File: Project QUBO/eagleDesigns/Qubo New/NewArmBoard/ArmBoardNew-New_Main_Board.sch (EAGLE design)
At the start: 13 parts, among them U1 BME280

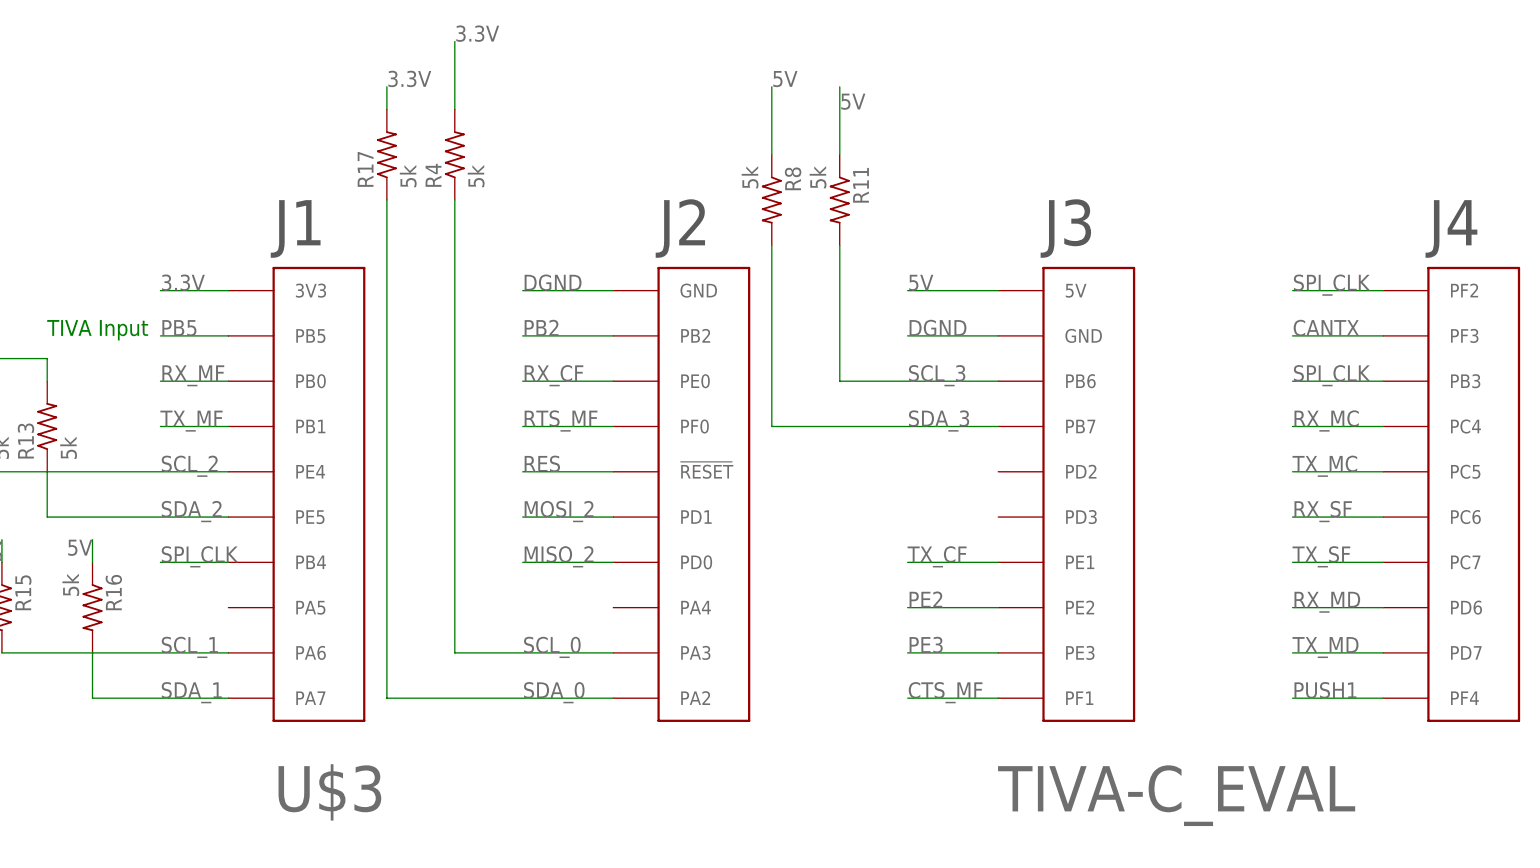
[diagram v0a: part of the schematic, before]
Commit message: Fixes to TIVA board
Some of the pins were named wrong so I fixed them
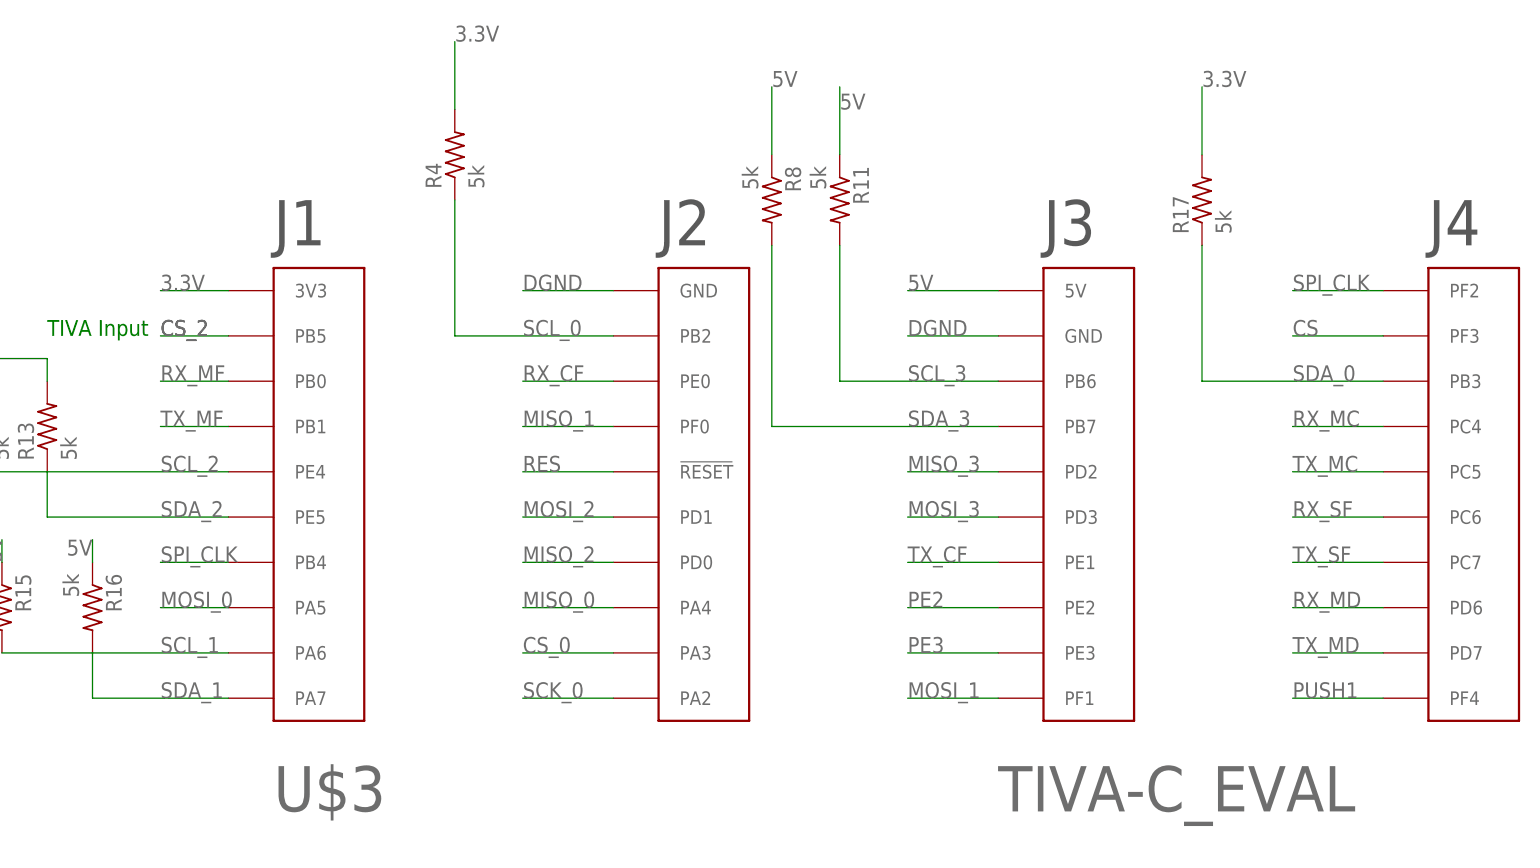
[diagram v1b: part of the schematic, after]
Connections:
- net CANTX renamed CS
- net CTS_MF renamed MOSI_1
- net PB5 renamed CS_2
- net RTS_MF renamed MISO_1
- removed net PB2: U$3.PB2
- new net CS_0: U$3.PA3
- new net MISO_0: U$3.PA4
- new net MISO_3: U$3.PD2
- new net MOSI_0: U$3.PA5
- new net MOSI_3: U$3.PD3
- new net SCK_0: U$3.PA2
- net SCL_0: now also U$3.PB2; no longer U$3.PA3
- net SDA_0: now also U$3.PB3; no longer U$3.PA2
- net SPI_CLK: no longer U$3.PB3
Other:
- moved on the sheet: R17
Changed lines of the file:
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@@
 <instance part="R8" gate="G$1" x="223.52" y="190.5" rot="R270"/>
 <instance part="R11" gate="G$1" x="231.14" y="190.5" rot="R270"/>
-<instance part="R17" gate="G$1" x="180.34" y="195.58" rot="R90"/>
+<instance part="R17" gate="G$1" x="271.78" y="190.5" rot="R90"/>
 <instance part="JP1" gate="G$1" x="101.6" y="144.78"/>
 </instances>
@@
 </busses>
 <nets>
-<net name="PB5" class="0">
+<net name="CS_2" class="0">
 <segment>
 <pinref part="U$3" gate="G$1" pin="PB5"/>
 <wire x1="162.56" y1="175.26" x2="154.94" y2="175.26" width="0.1524" layer="91"/>
+<label x="154.94" y="175.26" size="1.778" layer="95"/>
 <label x="154.94" y="175.26" size="1.778" layer="95"/>
 </segment>
@@
 <label x="281.94" y="180.34" size="1.778" layer="95"/>
 </segment>
-<segment>
-<pinref part="U$3" gate="G$1" pin="PB3"/>
-<wire x1="292.1" y1="170.18" x2="281.94" y2="170.18" width="0.1524" layer="91"/>
-<label x="281.94" y="170.18" size="1.778" layer="95"/>
-</segment>
 </net>
 <net name="RX_MF" class="0">
@@
 <segment>
 <pinref part="R17" gate="G$1" pin="2"/>
-<wire x1="180.34" y1="200.66" x2="180.34" y2="203.2" width="0.1524" layer="91"/>
-<label x="180.34" y="203.2" size="1.778" layer="95"/>
+<wire x1="271.78" y1="195.58" x2="271.78" y2="203.2" width="0.1524" layer="91"/>
+<label x="271.78" y="203.2" size="1.778" layer="95"/>
 </segment>
 <segment>
@@
 </segment>
 </net>
-<net name="CTS_MF" class="0">
+<net name="MOSI_1" class="0">
 <segment>
 <pinref part="U$3" gate="G$1" pin="PF1"/>
@@
 </segment>
 </net>
-<net name="RTS_MF" class="0">
+<net name="MISO_1" class="0">
 <segment>
 <pinref part="U$3" gate="G$1" pin="PF0"/>
@@
 </segment>
 </net>
-<net name="CANTX" class="0">
+<net name="CS" class="0">
 <segment>
 <pinref part="U$3" gate="G$1" pin="PF3"/>
@@
 </segment>
 <segment>
-<pinref part="U$3" gate="G$1" pin="PA3"/>
-<wire x1="205.74" y1="139.7" x2="187.96" y2="139.7" width="0.1524" layer="91"/>
-<label x="195.58" y="139.7" size="1.778" layer="95"/>
+<pinref part="U$3" gate="G$1" pin="PB2"/>
+<wire x1="205.74" y1="175.26" x2="187.96" y2="175.26" width="0.1524" layer="91"/>
+<label x="195.58" y="175.26" size="1.778" layer="95"/>
 <pinref part="R4" gate="G$1" pin="1"/>
-<wire x1="187.96" y1="190.5" x2="187.96" y2="139.7" width="0.1524" layer="91"/>
+<wire x1="187.96" y1="190.5" x2="187.96" y2="175.26" width="0.1524" layer="91"/>
 </segment>
 </net>
@@
 </segment>
 <segment>
-<pinref part="U$3" gate="G$1" pin="PA2"/>
-<label x="195.58" y="134.62" size="1.778" layer="95"/>
-<wire x1="205.74" y1="134.62" x2="180.34" y2="134.62" width="0.1524" layer="91"/>
+<pinref part="U$3" gate="G$1" pin="PB3"/>
+<label x="281.94" y="170.18" size="1.778" layer="95"/>
 <pinref part="R17" gate="G$1" pin="1"/>
-<wire x1="180.34" y1="134.62" x2="180.34" y2="190.5" width="0.1524" layer="91"/>
+<wire x1="271.78" y1="185.42" x2="271.78" y2="170.18" width="0.1524" layer="91"/>
+<wire x1="271.78" y1="170.18" x2="292.1" y2="170.18" width="0.1524" layer="91"/>
 </segment>
 </net>
@@
 </segment>
 </net>
-<net name="PB2" class="0">
-<segment>
-<pinref part="U$3" gate="G$1" pin="PB2"/>
-<wire x1="205.74" y1="175.26" x2="195.58" y2="175.26" width="0.1524" layer="91"/>
-<label x="195.58" y="175.26" size="1.778" layer="95"/>
-</segment>
-</net>
+<net name="MISO_3" class="0">
+<segment>
+<pinref part="U$3" gate="G$1" pin="PD2"/>
+<wire x1="248.92" y1="160.02" x2="238.76" y2="160.02" width="0.1524" layer="91"/>
+<label x="238.76" y="160.02" size="1.778" layer="95"/>
+</segment>
+</net>
+<net name="MOSI_3" class="0">
+<segment>
+<pinref part="U$3" gate="G$1" pin="PD3"/>
+<wire x1="248.92" y1="154.94" x2="238.76" y2="154.94" width="0.1524" layer="91"/>
+<label x="238.76" y="154.94" size="1.778" layer="95"/>
+</segment>
+</net>
+<net name="MISO_0" class="0">
+<segment>
+<pinref part="U$3" gate="G$1" pin="PA4"/>
+<wire x1="205.74" y1="144.78" x2="195.58" y2="144.78" width="0.1524" layer="91"/>
+<label x="195.58" y="144.78" size="1.778" layer="95"/>
+</segment>
+</net>
+<net name="CS_0" class="0">
+<segment>
+<pinref part="U$3" gate="G$1" pin="PA3"/>
+<wire x1="205.74" y1="139.7" x2="195.58" y2="139.7" width="0.1524" layer="91"/>
+<label x="195.58" y="139.7" size="1.778" layer="95"/>
+</segment>
+</net>
+<net name="SCK_0" class="0">
+<segment>
+<pinref part="U$3" gate="G$1" pin="PA2"/>
+<wire x1="205.74" y1="134.62" x2="195.58" y2="134.62" width="0.1524" layer="91"/>
+<label x="195.58" y="134.62" size="1.778" layer="95"/>
+</segment>
+</net>
+<net name="MOSI_0" class="0">
+<segment>
+<pinref part="U$3" gate="G$1" pin="PA5"/>
+<wire x1="162.56" y1="144.78" x2="154.94" y2="144.78" width="0.1524" layer="91"/>
+<label x="154.94" y="144.78" size="1.778" layer="95"/>
+</segment>
+</net>

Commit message: Changes to Tiva board
I had to rewire some things
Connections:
- new net SPI_CLK_2: U$3.PB4
- net 3.3V: now also R15.1, R16.1, U$1.9; no longer R17.2, R4.2
- net 5V: now also R17.2, R4.2; no longer R15.1, R16.1
- net N$9: no longer U$1.9
- net SCL_0: no longer U1.SCK/SCL
- net SCL_1: now also U1.SCK/SCL
- net SDA_0: no longer U1.SDI/SDA
- net SDA_1: now also U1.SDI/SDA
- net SPI_CLK: no longer U$3.PB4
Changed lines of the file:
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@@
 <net name="SPI_CLK" class="0">
-<segment>
-<pinref part="U$3" gate="G$1" pin="PB4"/>
-<wire x1="162.56" y1="149.86" x2="154.94" y2="149.86" width="0.1524" layer="91"/>
-<label x="154.94" y="149.86" size="1.778" layer="95"/>
-</segment>
 <segment>
 <pinref part="U$3" gate="G$1" pin="PF2"/>
@@
 </segment>
 <segment>
-<pinref part="R17" gate="G$1" pin="2"/>
-<wire x1="271.78" y1="195.58" x2="271.78" y2="203.2" width="0.1524" layer="91"/>
-<label x="271.78" y="203.2" size="1.778" layer="95"/>
-</segment>
-<segment>
-<pinref part="R4" gate="G$1" pin="2"/>
-<wire x1="187.96" y1="200.66" x2="187.96" y2="208.28" width="0.1524" layer="91"/>
-<label x="187.96" y="208.28" size="1.778" layer="95"/>
+<wire x1="147.32" y1="149.86" x2="147.32" y2="152.4" width="0.1524" layer="91"/>
+<label x="147.32" y="152.4" size="1.778" layer="95" rot="R180"/>
+<pinref part="R16" gate="G$1" pin="1"/>
+</segment>
+<segment>
+<wire x1="137.16" y1="149.86" x2="137.16" y2="152.4" width="0.1524" layer="91"/>
+<label x="137.16" y="149.86" size="1.778" layer="95" rot="R90"/>
+<pinref part="R15" gate="G$1" pin="1"/>
+</segment>
+<segment>
+<pinref part="U$1" gate="G$1" pin="9"/>
+<wire x1="177.8" y1="48.26" x2="170.18" y2="48.26" width="0.1524" layer="91"/>
+<label x="170.18" y="48.26" size="1.778" layer="95"/>
 </segment>
 </net>
@@
 </segment>
 <segment>
-<wire x1="137.16" y1="149.86" x2="137.16" y2="152.4" width="0.1524" layer="91"/>
-<label x="137.16" y="149.86" size="1.778" layer="95" rot="R90"/>
-<pinref part="R15" gate="G$1" pin="1"/>
-</segment>
-<segment>
-<wire x1="147.32" y1="149.86" x2="147.32" y2="152.4" width="0.1524" layer="91"/>
-<label x="147.32" y="152.4" size="1.778" layer="95" rot="R180"/>
-<pinref part="R16" gate="G$1" pin="1"/>
-</segment>
-<segment>
 <pinref part="U$3" gate="G$1" pin="5V"/>
 <wire x1="248.92" y1="180.34" x2="238.76" y2="180.34" width="0.1524" layer="91"/>
@@
 <label x="88.9" y="147.32" size="1.778" layer="95"/>
 </segment>
+<segment>
+<pinref part="R4" gate="G$1" pin="2"/>
+<wire x1="187.96" y1="200.66" x2="187.96" y2="208.28" width="0.1524" layer="91"/>
+<label x="187.96" y="208.28" size="1.778" layer="95"/>
+</segment>
+<segment>
+<pinref part="R17" gate="G$1" pin="2"/>
+<wire x1="271.78" y1="195.58" x2="271.78" y2="203.2" width="0.1524" layer="91"/>
+<label x="271.78" y="203.2" size="1.778" layer="95"/>
+</segment>
 </net>
 <net name="RES" class="0">
@@
 </net>
 <net name="N$9" class="0">
-<segment>
-<pinref part="U$1" gate="G$1" pin="9"/>
-<wire x1="177.8" y1="48.26" x2="170.18" y2="48.26" width="0.1524" layer="91"/>
-<label x="170.18" y="48.26" size="1.778" layer="95"/>
-</segment>
 <segment>
 <pinref part="U$2" gate="G$1" pin="9"/>
@@
 <pinref part="R15" gate="G$1" pin="2"/>
 <label x="154.94" y="139.7" size="1.778" layer="95"/>
+</segment>
+<segment>
+<pinref part="U1" gate="U1" pin="SCK/SCL"/>
+<wire x1="281.94" y1="53.34" x2="289.56" y2="53.34" width="0.1524" layer="91"/>
+<label x="281.94" y="53.34" size="1.778" layer="95"/>
 </segment>
 </net>
@@
 <label x="154.94" y="134.62" size="1.778" layer="95"/>
 </segment>
+<segment>
+<pinref part="U1" gate="U1" pin="SDI/SDA"/>
+<wire x1="281.94" y1="58.42" x2="289.56" y2="58.42" width="0.1524" layer="91"/>
+<label x="281.94" y="58.42" size="1.778" layer="95"/>
+</segment>
 </net>
 <net name="MISO_2" class="0">
@@
 <wire x1="177.8" y1="58.42" x2="170.18" y2="58.42" width="0.1524" layer="91"/>
 <label x="165.1" y="58.42" size="1.778" layer="95"/>
-</segment>
-<segment>
-<pinref part="U1" gate="U1" pin="SCK/SCL"/>
-<wire x1="281.94" y1="53.34" x2="289.56" y2="53.34" width="0.1524" layer="91"/>
-<label x="281.94" y="53.34" size="1.778" layer="95"/>
 </segment>
 <segment>
@@
 </segment>
 <segment>
-<pinref part="U1" gate="U1" pin="SDI/SDA"/>
-<wire x1="281.94" y1="58.42" x2="289.56" y2="58.42" width="0.1524" layer="91"/>
-<label x="281.94" y="58.42" size="1.778" layer="95"/>
-</segment>
-<segment>
 <pinref part="U$3" gate="G$1" pin="PB3"/>
 <label x="281.94" y="170.18" size="1.778" layer="95"/>
@@
 </segment>
 </net>
+<net name="SPI_CLK_2" class="0">
+<segment>
+<pinref part="U$3" gate="G$1" pin="PB4"/>
+<wire x1="162.56" y1="149.86" x2="154.94" y2="149.86" width="0.1524" layer="91"/>
+<label x="154.94" y="149.86" size="1.778" layer="95"/>
+</segment>
+</net>
